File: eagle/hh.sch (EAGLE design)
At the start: 7 parts

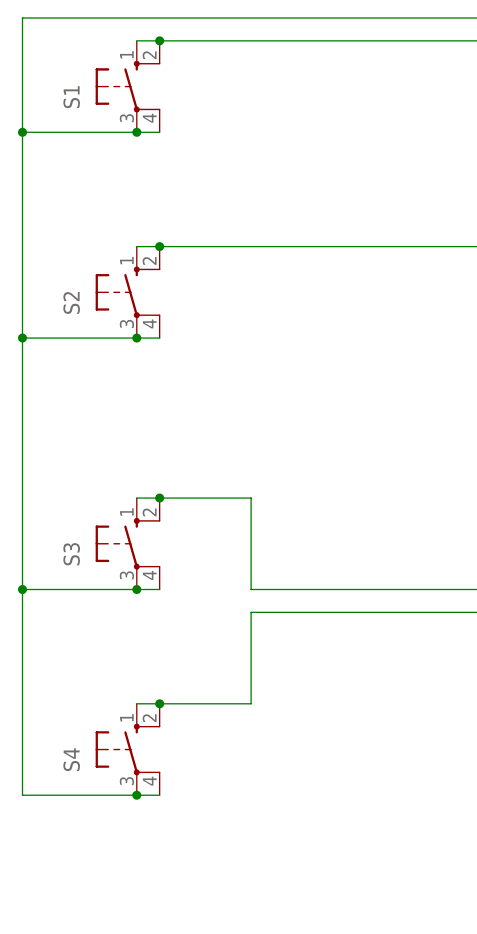
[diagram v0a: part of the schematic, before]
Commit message: Major changes to placement of components
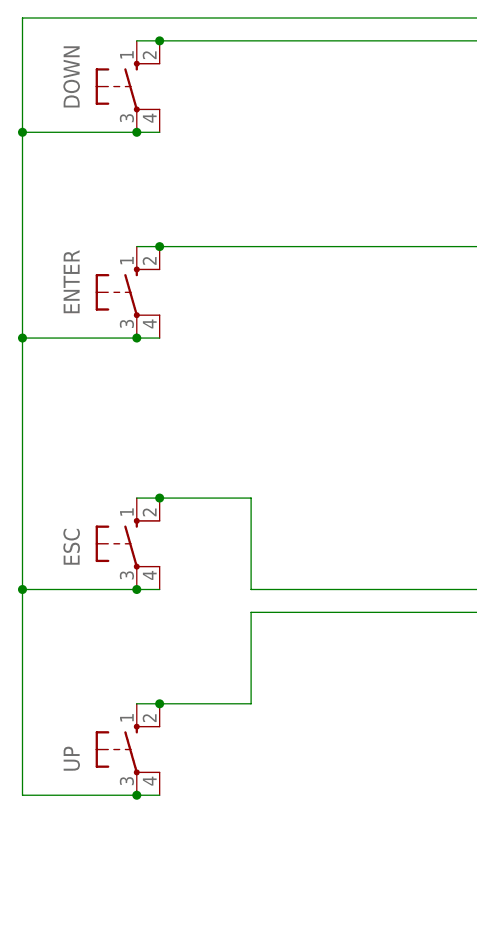
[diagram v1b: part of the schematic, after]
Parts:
- renumbered S1 to DOWN, S2 to ENTER, S3 to ESC, S4 to UP
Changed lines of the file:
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@@
 </classes>
 <parts>
-<part name="S1" library="switch-omron" deviceset="10-XX" device=""/>
-<part name="S2" library="switch-omron" deviceset="10-XX" device=""/>
-<part name="S3" library="switch-omron" deviceset="10-XX" device=""/>
-<part name="S4" library="switch-omron" deviceset="10-XX" device=""/>
+<part name="DOWN" library="switch-omron" deviceset="10-XX" device=""/>
+<part name="ENTER" library="switch-omron" deviceset="10-XX" device=""/>
+<part name="ESC" library="switch-omron" deviceset="10-XX" device=""/>
+<part name="UP" library="switch-omron" deviceset="10-XX" device=""/>
 <part name="ESP12E_DEVKIT" library="ESP12E_DEVKIT" deviceset="ESP12E_DEVKIT" device=""/>
 <part name="FRAME1" library="frames" deviceset="FRAME_A_L" device=""/>
@@
 </plain>
 <instances>
-<instance part="S1" gate="1" x="22.86" y="142.24"/>
-<instance part="S2" gate="1" x="22.86" y="119.38"/>
-<instance part="S3" gate="1" x="22.86" y="91.44"/>
-<instance part="S4" gate="1" x="22.86" y="68.58"/>
+<instance part="DOWN" gate="1" x="22.86" y="142.24"/>
+<instance part="ENTER" gate="1" x="22.86" y="119.38"/>
+<instance part="ESC" gate="1" x="22.86" y="91.44"/>
+<instance part="UP" gate="1" x="22.86" y="68.58"/>
 <instance part="ESP12E_DEVKIT" gate="G$1" x="119.38" y="93.98" rot="R180"/>
 <instance part="FRAME1" gate="G$1" x="-22.86" y="-12.7"/>
@@
 <segment>
 <pinref part="ESP12E_DEVKIT" gate="G$1" pin="D3"/>
-<pinref part="S4" gate="1" pin="S1"/>
+<pinref part="UP" gate="1" pin="S1"/>
 <wire x1="101.6" y1="83.82" x2="35.56" y2="83.82" width="0.1524" layer="91"/>
 <wire x1="35.56" y1="83.82" x2="35.56" y2="73.66" width="0.1524" layer="91"/>
 <wire x1="35.56" y1="73.66" x2="25.4" y2="73.66" width="0.1524" layer="91"/>
-<pinref part="S4" gate="1" pin="S"/>
+<pinref part="UP" gate="1" pin="S"/>
 <wire x1="22.86" y1="73.66" x2="25.4" y2="73.66" width="0.1524" layer="91"/>
 <junction x="25.4" y="73.66"/>
@@
 <segment>
 <pinref part="ESP12E_DEVKIT" gate="G$1" pin="D4"/>
-<pinref part="S3" gate="1" pin="S1"/>
+<pinref part="ESC" gate="1" pin="S1"/>
 <wire x1="101.6" y1="86.36" x2="35.56" y2="86.36" width="0.1524" layer="91"/>
 <wire x1="35.56" y1="86.36" x2="35.56" y2="96.52" width="0.1524" layer="91"/>
 <wire x1="35.56" y1="96.52" x2="25.4" y2="96.52" width="0.1524" layer="91"/>
-<pinref part="S3" gate="1" pin="S"/>
+<pinref part="ESC" gate="1" pin="S"/>
 <wire x1="22.86" y1="96.52" x2="25.4" y2="96.52" width="0.1524" layer="91"/>
 <junction x="25.4" y="96.52"/>
@@
 <net name="N$8" class="0">
 <segment>
-<pinref part="S2" gate="1" pin="S1"/>
+<pinref part="ENTER" gate="1" pin="S1"/>
 <wire x1="60.96" y1="124.46" x2="25.4" y2="124.46" width="0.1524" layer="91"/>
-<pinref part="S2" gate="1" pin="S"/>
+<pinref part="ENTER" gate="1" pin="S"/>
 <wire x1="22.86" y1="124.46" x2="25.4" y2="124.46" width="0.1524" layer="91"/>
 <junction x="25.4" y="124.46"/>
@@
 <net name="N$9" class="0">
 <segment>
-<pinref part="S1" gate="1" pin="S1"/>
+<pinref part="DOWN" gate="1" pin="S1"/>
 <wire x1="63.5" y1="147.32" x2="25.4" y2="147.32" width="0.1524" layer="91"/>
-<pinref part="S1" gate="1" pin="S"/>
+<pinref part="DOWN" gate="1" pin="S"/>
 <wire x1="22.86" y1="147.32" x2="25.4" y2="147.32" width="0.1524" layer="91"/>
 <junction x="25.4" y="147.32"/>
@@
 <wire x1="66.04" y1="109.22" x2="66.04" y2="149.86" width="0.1524" layer="91"/>
 <junction x="101.6" y="109.22"/>
-<pinref part="S4" gate="1" pin="P"/>
+<pinref part="UP" gate="1" pin="P"/>
 <wire x1="22.86" y1="63.5" x2="10.16" y2="63.5" width="0.1524" layer="91"/>
 <wire x1="10.16" y1="63.5" x2="10.16" y2="86.36" width="0.1524" layer="91"/>
 <wire x1="10.16" y1="86.36" x2="10.16" y2="114.3" width="0.1524" layer="91"/>
 <wire x1="10.16" y1="114.3" x2="10.16" y2="137.16" width="0.1524" layer="91"/>
-<pinref part="S3" gate="1" pin="P"/>
+<pinref part="ESC" gate="1" pin="P"/>
 <wire x1="22.86" y1="86.36" x2="10.16" y2="86.36" width="0.1524" layer="91"/>
 <junction x="10.16" y="86.36"/>
-<pinref part="S2" gate="1" pin="P"/>
+<pinref part="ENTER" gate="1" pin="P"/>
 <wire x1="22.86" y1="114.3" x2="10.16" y2="114.3" width="0.1524" layer="91"/>
 <junction x="10.16" y="114.3"/>
-<pinref part="S1" gate="1" pin="P"/>
+<pinref part="DOWN" gate="1" pin="P"/>
 <wire x1="22.86" y1="137.16" x2="10.16" y2="137.16" width="0.1524" layer="91"/>
-<pinref part="S1" gate="1" pin="P1"/>
+<pinref part="DOWN" gate="1" pin="P1"/>
 <wire x1="25.4" y1="137.16" x2="22.86" y2="137.16" width="0.1524" layer="91"/>
 <junction x="22.86" y="137.16"/>
-<pinref part="S2" gate="1" pin="P1"/>
+<pinref part="ENTER" gate="1" pin="P1"/>
 <wire x1="25.4" y1="114.3" x2="22.86" y2="114.3" width="0.1524" layer="91"/>
 <junction x="22.86" y="114.3"/>
-<pinref part="S3" gate="1" pin="P1"/>
+<pinref part="ESC" gate="1" pin="P1"/>
 <wire x1="25.4" y1="86.36" x2="22.86" y2="86.36" width="0.1524" layer="91"/>
 <junction x="22.86" y="86.36"/>
-<pinref part="S4" gate="1" pin="P1"/>
+<pinref part="UP" gate="1" pin="P1"/>
 <wire x1="25.4" y1="63.5" x2="22.86" y2="63.5" width="0.1524" layer="91"/>
 <junction x="22.86" y="63.5"/>
